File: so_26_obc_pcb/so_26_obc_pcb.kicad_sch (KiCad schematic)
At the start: 49 parts, among them J1 Conn_02x12_Odd_Even, J2 Conn_02x06_Odd_Even, J3 Conn_01x04, J4 Conn_01x03, J5 Conn_01x03, J6 Conn_01x02, SW1 SW_Push, U1 STM32G431RBTx, U2 MPRLS0025, U3 PCT2075, U4 LSM6DS3, U5 MEM2067-02-180-00-A, U6 TPT3232A-TS3R

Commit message: review by aj
added max232cpe and other things
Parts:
- removed C17, C18, C19, C20, C21: 100n, Capacitor_SMD:C_0805_2012Metric_Pad1.18x1.45mm_HandSolder, symbol Device:C_Small
- removed U6: TPT3232A-TS3R, Package_SO:TSSOP-16_4.4x5mm_P0.65mm, symbol so_26_obc_library:TPT3232A-TS3R
- added C22: 100n, Capacitor_SMD:C_0805_2012Metric_Pad1.18x1.45mm_HandSolder, symbol Device:C_Small
- added C23, C24, C25, C26: 1u, Capacitor_SMD:C_0805_2012Metric_Pad1.18x1.45mm_HandSolder, symbol Device:C_Small
- added C27, C28: 10u, Capacitor_SMD:C_0805_2012Metric_Pad1.18x1.45mm_HandSolder, symbol Device:C_Small
- added D5: LED_PWR, LED_SMD:LED_0805_2012Metric_Pad1.15x1.40mm_HandSolder, symbol Device:LED_Small
- added JP1, JP2: SolderJumper_3_Open, Jumper:SolderJumper-3_P1.3mm_Open_Pad1.0x1.5mm, symbol Jumper:SolderJumper_3_Open
- added R12: 10k, Resistor_SMD:R_0805_2012Metric_Pad1.20x1.40mm_HandSolder, symbol Device:R_Small
- added U7: AMS1117-5.0, Package_TO_SOT_SMD:SOT-223-3_TabPin2, symbol Regulator_Linear:AMS1117-5.0
- added U8: MAX232, Package_DIP:DIP-16_W7.62mm, symbol Interface_UART:MAX232
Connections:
- net +10V: now also C28.1, U7.3 (VI)
- net GND: now also C22.2, C25.2, C27.2, C28.2, D5.1 (K), U7.1 (GND), U8.15 (GND)
- net RADIO_RX: now also U8.7 (T2OUT); no longer U1.23 (PC5)
- net RADIO_TX: now also U8.8 (R2IN); no longer U1.22 (PC4)
- new net: C24.2, U8.1 (C1+)
- new net: JP2.2 (C), U8.10 (T2IN)
- new net: C26.1, U8.2 (VS+)
- new net: C24.1, U8.3 (C1-)
- new net: C23.2, U8.4 (C2+)
- new net: C23.1, U8.5 (C2-)
- new net: C25.1, U8.6 (VS-)
- new net: JP1.2 (C), U8.9 (R2OUT)
- new net: D5.2 (A), R12.1
- new net +5V: C22.1, C26.2, C27.1, R12.2, U7.2 (VO), U8.16 (VCC)
- new net RADIO_UART_RX: JP1.3 (B), JP2.3 (B), U1.23 (PC5)
- new net RADIO_UART_TX: JP1.1 (A), JP2.1 (A), U1.22 (PC4)
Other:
- note removed: "Level shifter for radio"

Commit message: changed back to old rs232 tranceiver
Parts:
- removed C22: 100n, Capacitor_SMD:C_0805_2012Metric_Pad1.18x1.45mm_HandSolder, symbol Device:C_Small
- removed C23, C24, C25, C26: 1u, Capacitor_SMD:C_0805_2012Metric_Pad1.18x1.45mm_HandSolder, symbol Device:C_Small
- removed C27, C28: 10u, Capacitor_SMD:C_0805_2012Metric_Pad1.18x1.45mm_HandSolder, symbol Device:C_Small
- removed D5: LED_PWR, LED_SMD:LED_0805_2012Metric_Pad1.15x1.40mm_HandSolder, symbol Device:LED_Small
- removed JP1, JP2: SolderJumper_3_Open, Jumper:SolderJumper-3_P1.3mm_Open_Pad1.0x1.5mm, symbol Jumper:SolderJumper_3_Open
- removed R12: 10k, Resistor_SMD:R_0805_2012Metric_Pad1.20x1.40mm_HandSolder, symbol Device:R_Small
- removed U7: AMS1117-5.0, Package_TO_SOT_SMD:SOT-223-3_TabPin2, symbol Regulator_Linear:AMS1117-5.0
- removed U8: MAX232, Package_DIP:DIP-16_W7.62mm, symbol Interface_UART:MAX232
- added C11, C12, C14, C15, C16: 100n, Capacitor_SMD:C_0805_2012Metric_Pad1.18x1.45mm_HandSolder, symbol Device:C_Small
- added U2: TPT3232A-TS3R, Package_SO:TSSOP-16_4.4x5mm_P0.65mm, symbol so_26_obc_library:TPT3232A-TS3R
- renumbered C12 to C13, C14 to C17, C11 to C18, C16 to C19, C15 to C20, C13 to C21, J6 to J5, J5 to J6, R9 to R10, R10 to R11, R11 to R7, R7 to R8, R8 to R9, U2 to U4, U4 to U5, U5 to U6
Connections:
- net +3V3: now also C11.1, U2.16 (VCC), U2.8 (RIN2)
- net GND: now also C11.2, C15.2, C16.1, U2.10 (TIN2), U2.15 (GND)
- net RADIO_RX: now also U2.13 (RIN1)
- net RADIO_TX: now also U2.14 (TOUT1)
- net RADIO_UART_RX: now also U2.12 (ROUT1)
- net RADIO_UART_TX: now also U2.11 (TIN1)
- new net: C16.2, U2.2 (V+)
- new net: C14.1, U2.5 (C2-)
- new net: C14.2, U2.4 (C2+)
- new net: C12.1, U2.3 (C1-)
- new net: C12.2, U2.1 (C1+)
- new net: C15.1, U2.6 (V-)
- no-connect marks 48 -> 46
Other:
- note added: "UART-RS232"
- moved on the sheet: C1, D2, J1, R2

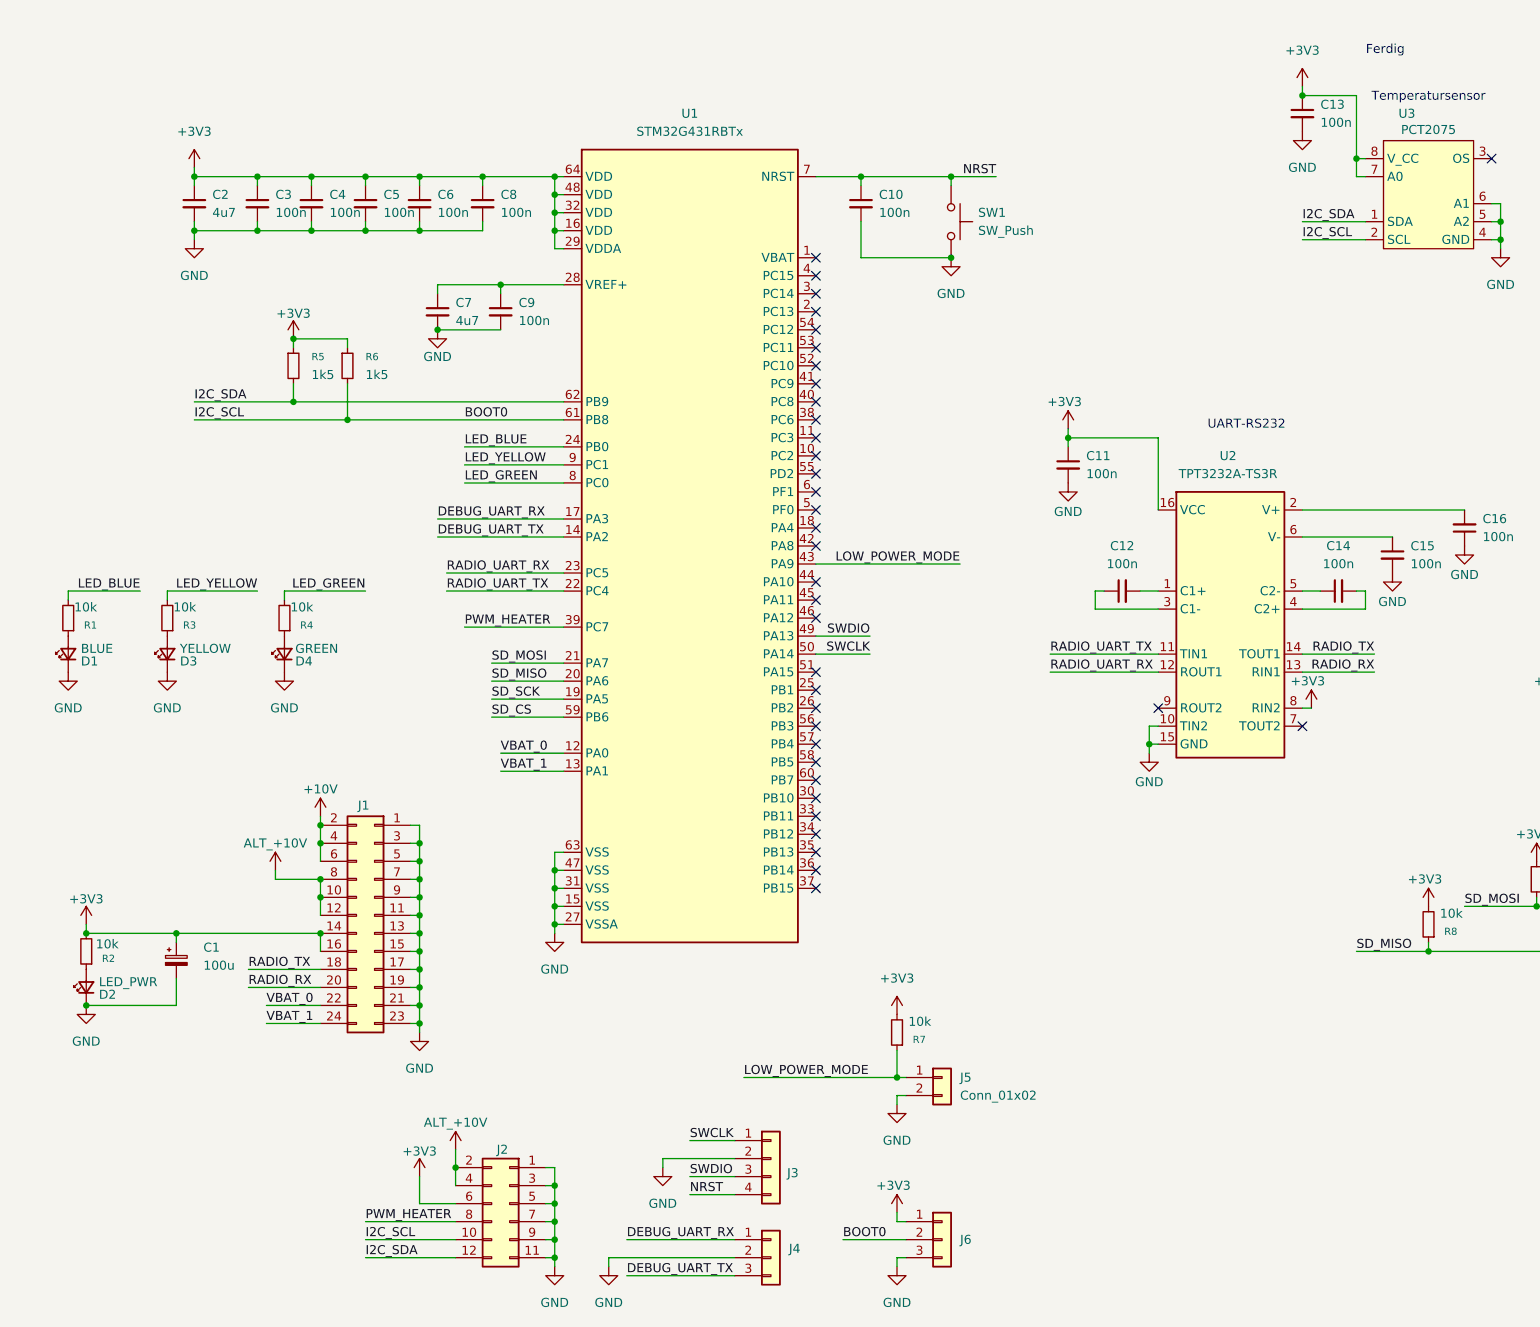
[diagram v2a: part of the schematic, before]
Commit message: Schematic: Added connector symbols for code debugging
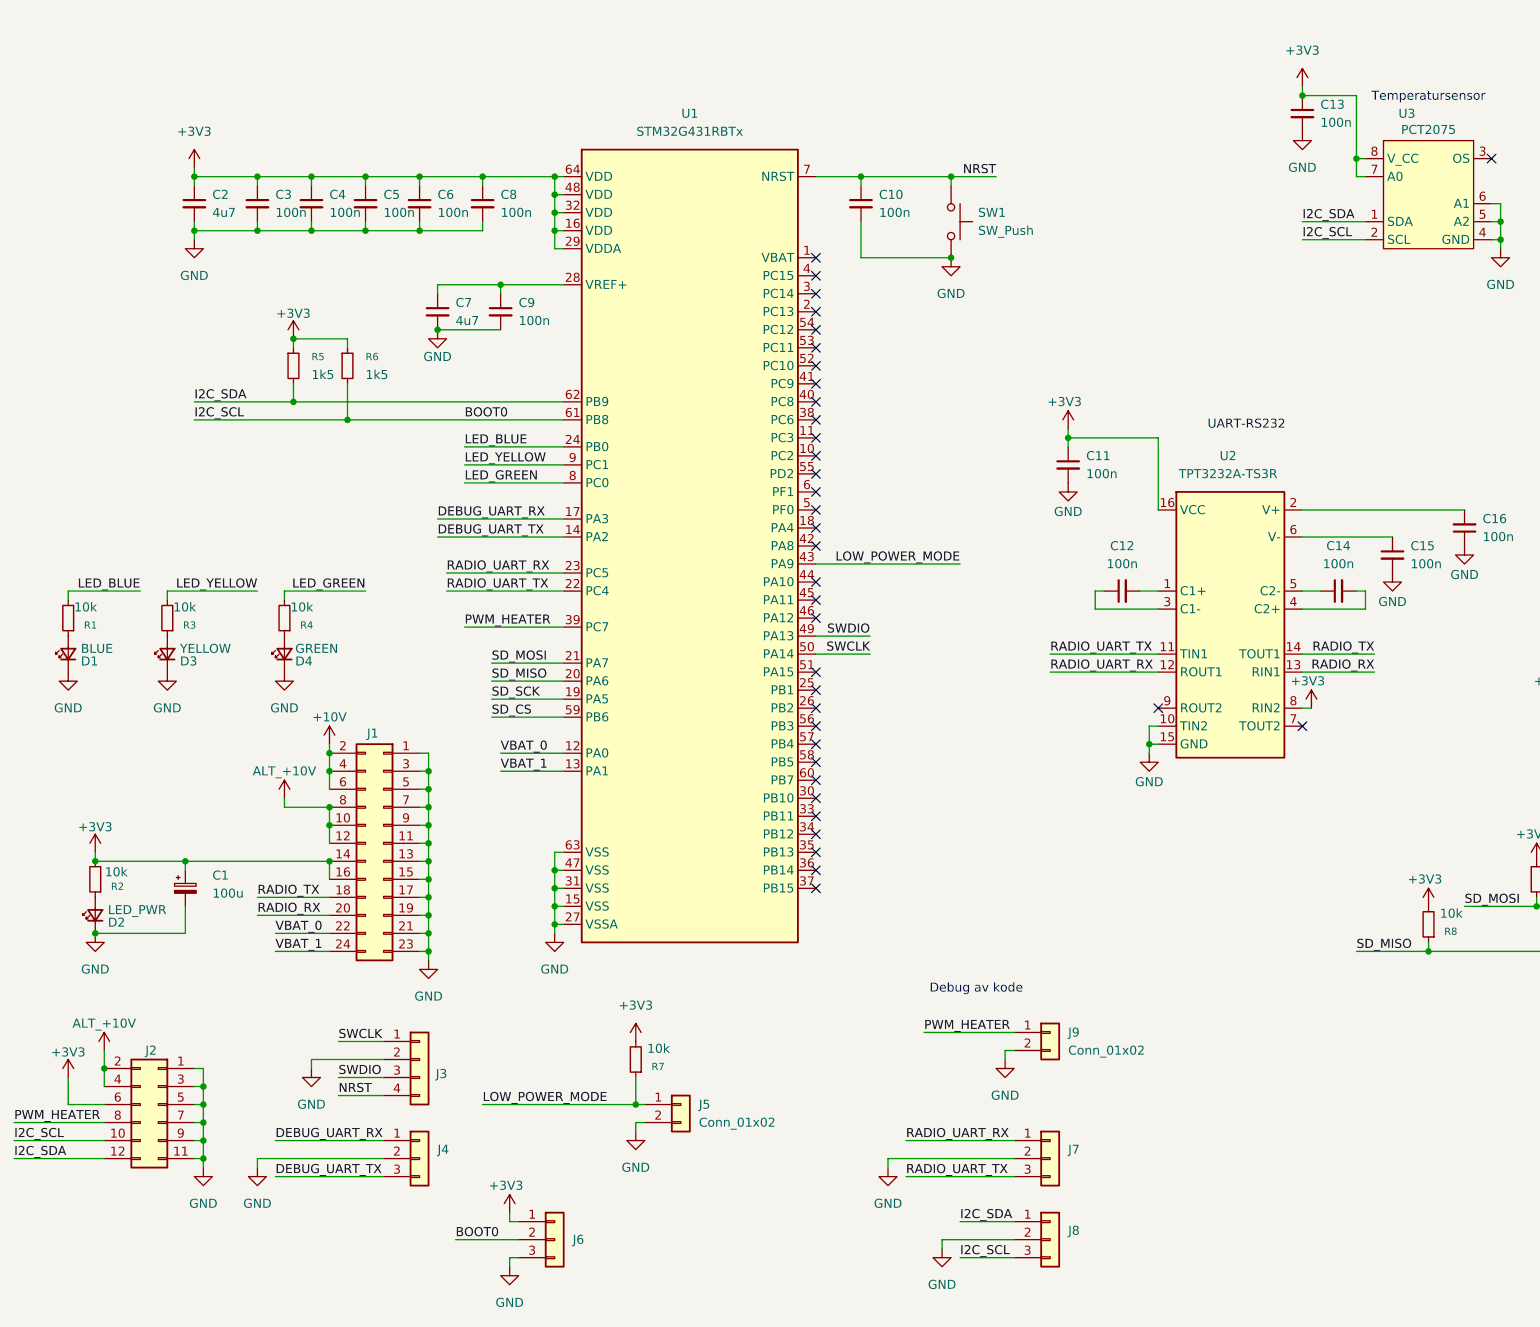
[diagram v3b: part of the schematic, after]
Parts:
- added J7, J8: Conn_01x03, Connector_PinHeader_2.54mm:PinHeader_1x03_P2.54mm_Vertical, symbol Connector_Generic:Conn_01x03
- added J9: Conn_01x02, Connector_PinSocket_2.54mm:PinSocket_1x02_P2.54mm_Vertical, symbol Connector_Generic:Conn_01x02
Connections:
- net BOOT0: now also J8.3 (Pin_3)
- net GND: now also J7.2 (Pin_2), J8.2 (Pin_2), J9.2 (Pin_2)
- net I2C_SDA: now also J8.1 (Pin_1)
- net PWM_HEATER: now also J9.1 (Pin_1)
- net RADIO_UART_RX: now also J7.1 (Pin_1)
- net RADIO_UART_TX: now also J7.3 (Pin_3)
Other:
- note added: "Debug av kode"
- note removed: "Ferdig"
- moved on the sheet: C1, D2, J1, J2, J3, J4, J5, J6, R2, R7

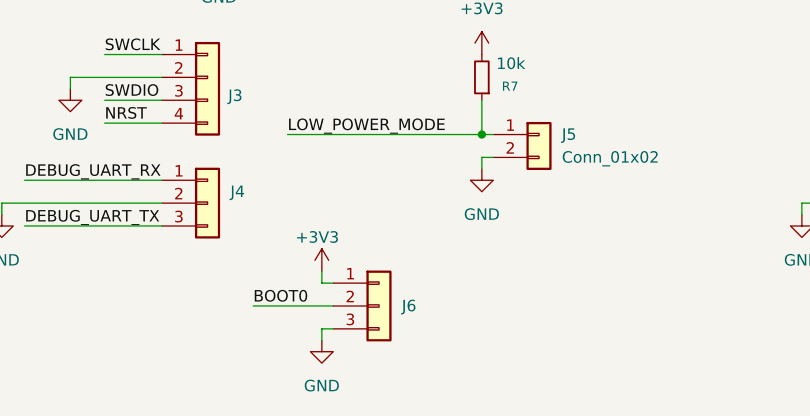
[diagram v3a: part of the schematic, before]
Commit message: PCB: Routed before cleanup by AJ
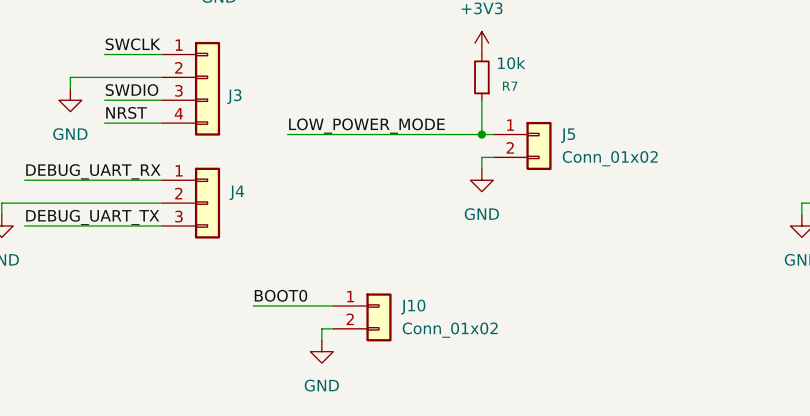
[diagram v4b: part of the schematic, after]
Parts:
- removed J6: Conn_01x03, Connector_PinHeader_2.54mm:PinHeader_1x03_P2.54mm_Vertical, symbol Connector_Generic:Conn_01x03
- added J10: Conn_01x02, Connector_PinSocket_2.54mm:PinSocket_1x02_P2.54mm_Vertical, symbol Connector_Generic:Conn_01x02
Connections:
- net BOOT0: now also J10.1 (Pin_1)
- net GND: now also J10.2 (Pin_2)
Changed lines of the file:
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@@
 	(wire
 		(pts
-			(xy 85.09 185.42) (xy 85.09 184.15)
-		)
-		(stroke
-			(width 0)
-			(type default)
-		)
-	)
-	(wire
-		(pts
 			(xy 205.74 96.52) (xy 204.47 96.52)
 		)
@@
 	(wire
 		(pts
-			(xy 85.09 185.42) (xy 86.36 185.42)
-		)
-		(stroke
-			(width 0)
-			(type default)
-		)
-	)
-	(wire
-		(pts
 			(xy 223.52 44.45) (xy 224.79 44.45)
 		)
@@
 	)
 	(symbol
+		(lib_id "Connector_Generic:Conn_01x02")
+		(at 91.44 187.96 0)
+		(unit 1)
+		(exclude_from_sim no)
+		(in_bom yes)
+		(on_board yes)
+		(dnp no)
+		(fields_autoplaced yes)
+		(property "Reference" "J10"
+			(at 93.98 187.9599 0)
+			(effects
+				(font
+					(size 1.27 1.27)
+				)
+				(justify left)
+			)
+		)
+		(property "Value" "Conn_01x02"
+			(at 93.98 190.4999 0)
+			(effects
+				(font
+					(size 1.27 1.27)
+				)
+				(justify left)
+			)
+		)
+		(property "Footprint" "Connector_PinSocket_2.54mm:PinSocket_1x02_P2.54mm_Vertical"
+			(at 91.44 187.96 0)
+			(effects
+				(font
+					(size 1.27 1.27)
+				)
+				(hide yes)
+			)
+		)
+		(property "Datasheet" "~"
+			(at 91.44 187.96 0)
+			(effects
+				(font
+					(size 1.27 1.27)
+				)
+				(hide yes)
+			)
+		)
+		(property "Description" "Generic connector, single row, 01x02, script generated (kicad-library-utils/schlib/autogen/connector/)"
+			(at 91.44 187.96 0)
+			(effects
+				(font
+					(size 1.27 1.27)
+				)
+				(hide yes)
+			)
+		)
+		(pin "2"
+		)
+		(pin "1"
+		)
+		(instances
+			(project "so_26_obc_pcb"
+				(path "/19e03f49-67e8-4e0c-a53b-de9e8097c0a8"
+					(reference "J10")
+					(unit 1)
+				)
+			)
+		)
+	)
+	(symbol
 		(lib_id "so_26_obc_library:LSM6DS3TR")
 		(at 269.24 15.24 0)
@@
 	)
 	(symbol
-		(lib_id "power:+3V3")
-		(at 85.09 184.15 0)
-		(unit 1)
-		(exclude_from_sim no)
-		(in_bom yes)
-		(on_board yes)
-		(dnp no)
-		(property "Reference" "#PWR021"
-			(at 85.09 187.96 0)
-			(effects
-				(font
-					(size 1.27 1.27)
-				)
-				(hide yes)
-			)
-		)
-		(property "Value" "+3V3"
-			(at 84.582 180.34 0)
-			(effects
-				(font
-					(size 1.27 1.27)
-				)
-			)
-		)
-		(property "Footprint" ""
-			(at 85.09 184.15 0)
-			(effects
-				(font
-					(size 1.27 1.27)
-				)
-				(hide yes)
-			)
-		)
-		(property "Datasheet" ""
-			(at 85.09 184.15 0)
-			(effects
-				(font
-					(size 1.27 1.27)
-				)
-				(hide yes)
-			)
-		)
-		(property "Description" "Power symbol creates a global label with name \"+3V3\""
-			(at 85.09 184.15 0)
-			(effects
-				(font
-					(size 1.27 1.27)
-				)
-				(hide yes)
-			)
-		)
-		(pin "1"
-		)
-		(instances
-			(project "so_26_obc_pcb"
-				(path "/19e03f49-67e8-4e0c-a53b-de9e8097c0a8"
-					(reference "#PWR021")
-					(unit 1)
-				)
-			)
-		)
-	)
-	(symbol
 		(lib_id "Device:C_Small")
 		(at 171.45 96.52 90)
@@
 					(unit 1)
 				)
-			)
-		)
-	)
-	(symbol
-		(lib_id "Connector_Generic:Conn_01x03")
-		(at 91.44 187.96 0)
-		(unit 1)
-		(exclude_from_sim no)
-		(in_bom yes)
-		(on_board yes)
-		(dnp no)
-		(fields_autoplaced yes)
-		(property "Reference" "J6"
-			(at 93.98 187.9599 0)
-			(effects
-				(font
-					(size 1.27 1.27)
-				)
-				(justify left)
-			)
-		)
-		(property "Value" "Conn_01x03"
-			(at 93.98 189.2299 0)
-			(effects
-				(font
-					(size 1.27 1.27)
-				)
-				(justify left)
-				(hide yes)
-			)
-		)
-		(property "Footprint" "Connector_PinHeader_2.54mm:PinHeader_1x03_P2.54mm_Vertical"
-			(at 91.44 187.96 0)
-			(effects
-				(font
-					(size 1.27 1.27)
-				)
-				(hide yes)
-			)
-		)
-		(property "Datasheet" "~"
-			(at 91.44 187.96 0)
-			(effects
-				(font
-					(size 1.27 1.27)
-				)
-				(hide yes)
-			)
-		)
-		(property "Description" "Generic connector, single row, 01x03, script generated (kicad-library-utils/schlib/autogen/connector/)"
-			(at 91.44 187.96 0)
-			(effects
-				(font
-					(size 1.27 1.27)
-				)
-				(hide yes)
-			)
-		)
-		(pin "1"
-		)
-		(pin "3"
-		)
-		(pin "2"
-		)
-		(instances
-			(project "so_26_obc_pcb"
-				(path "/19e03f49-67e8-4e0c-a53b-de9e8097c0a8"
-					(reference "J6")
-					(unit 1)
-				)
